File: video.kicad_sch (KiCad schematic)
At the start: 89 parts, among them Q10 2N3906, Q4 2N3906, Q5 2N3906, Q6 2N3906, Q7 2N3906, Q8 2N3906, Q9 2N3906

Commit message: prepare for fabrication
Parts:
- C41, C42, C51, C52, C53, C61: LCSC (none) -> C46653; LCSC Part (none) -> C46653
- C43, C44, C63, C72, C81: LCSC (none) -> C344201; LCSC Part (none) -> C344201
- C45, C54, C55, C56, C57, C58: LCSC (none) -> C113833; LCSC Part (none) -> C113833
- C46, C47, C48: LCSC (none) -> C107154; LCSC Part (none) -> C107154
- Q10, Q4, Q5, Q6, Q7, Q8, Q9: LCSC (none) -> C49023424; LCSC Part (none) -> C49023424
- R22, R24, R25, R26, R35, R36, R38, R39: LCSC (none) -> C2907326; LCSC Part (none) -> C2907326
- R23: LCSC (none) -> C2907216; LCSC Part (none) -> C2907216
- R27, R29, R31, R33, R37, R41, R53, R54: LCSC (none) -> C137498; LCSC Part (none) -> C137498
- R28, R40, R55: LCSC (none) -> C17540; LCSC Part (none) -> C17540
- R30, R32, R34: LCSC (none) -> C17634; LCSC Part (none) -> C17634
- R42, R43, R44, R45, R47: LCSC (none) -> C4368; LCSC Part (none) -> C4368
- R46: LCSC (none) -> C2907268; LCSC Part (none) -> C2907268
- R48: LCSC (none) -> C149504; LCSC Part (none) -> C149504
- R57, R58, R59: LCSC (none) -> C2483588; LCSC Part (none) -> C2483588
- R70: LCSC (none) -> C2907219; LCSC Part (none) -> C2907219
- TP16, TP17, TP18, TP19, TP20, TP21, TP22, TP23, TP24, TP25, TP26, TP28, TP29, TP41: now not fitted

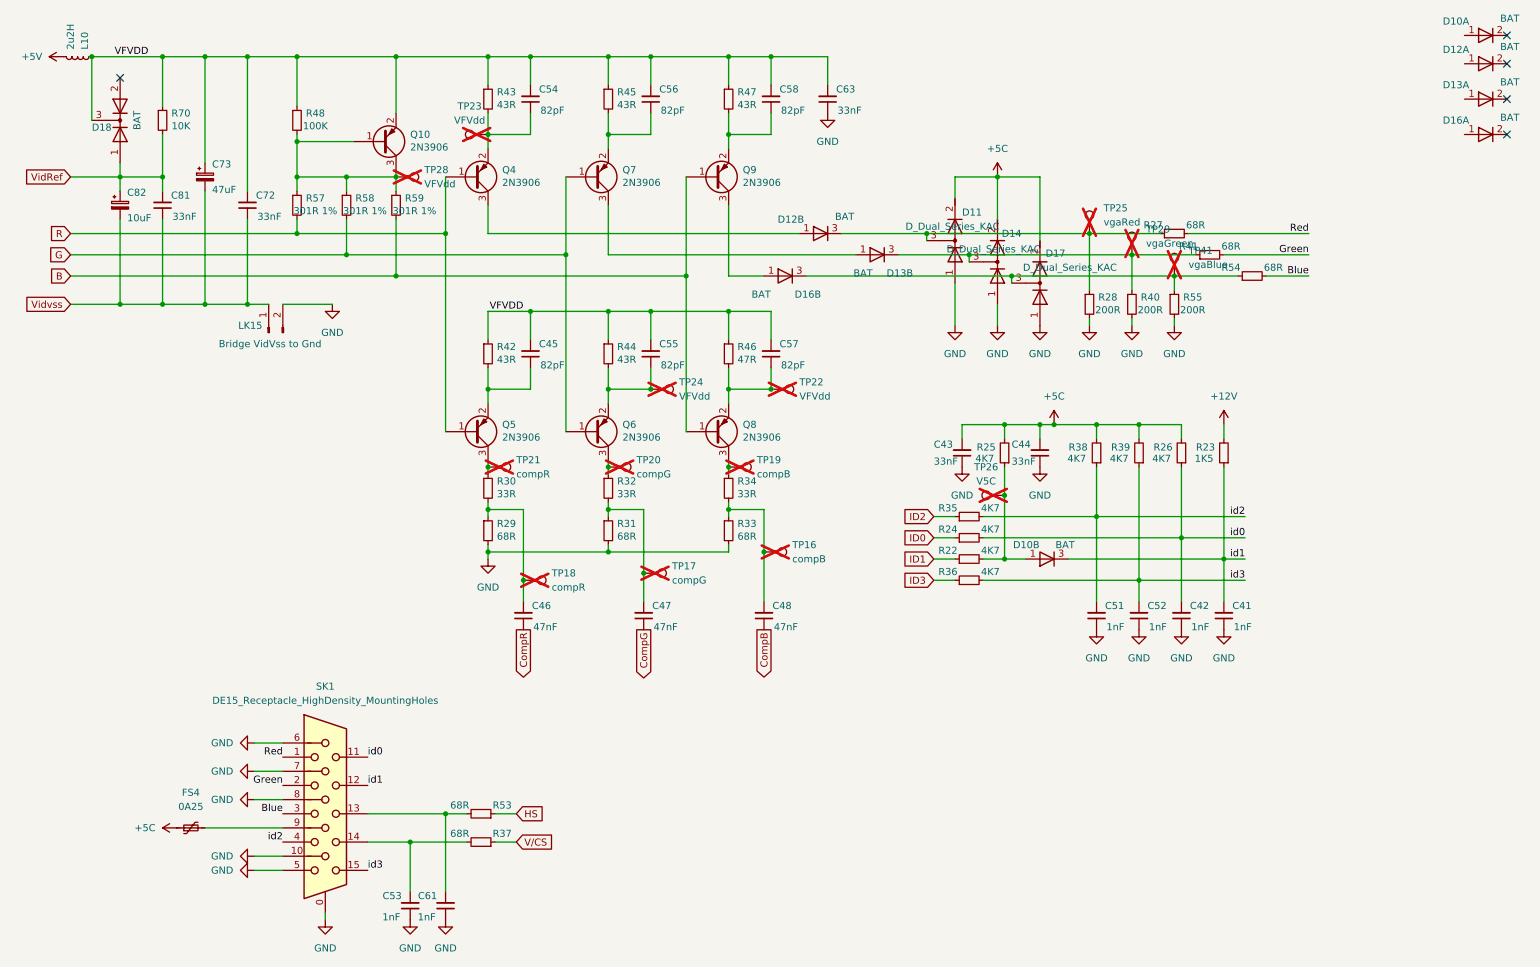
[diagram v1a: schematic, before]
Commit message: verify all component values vs TRM
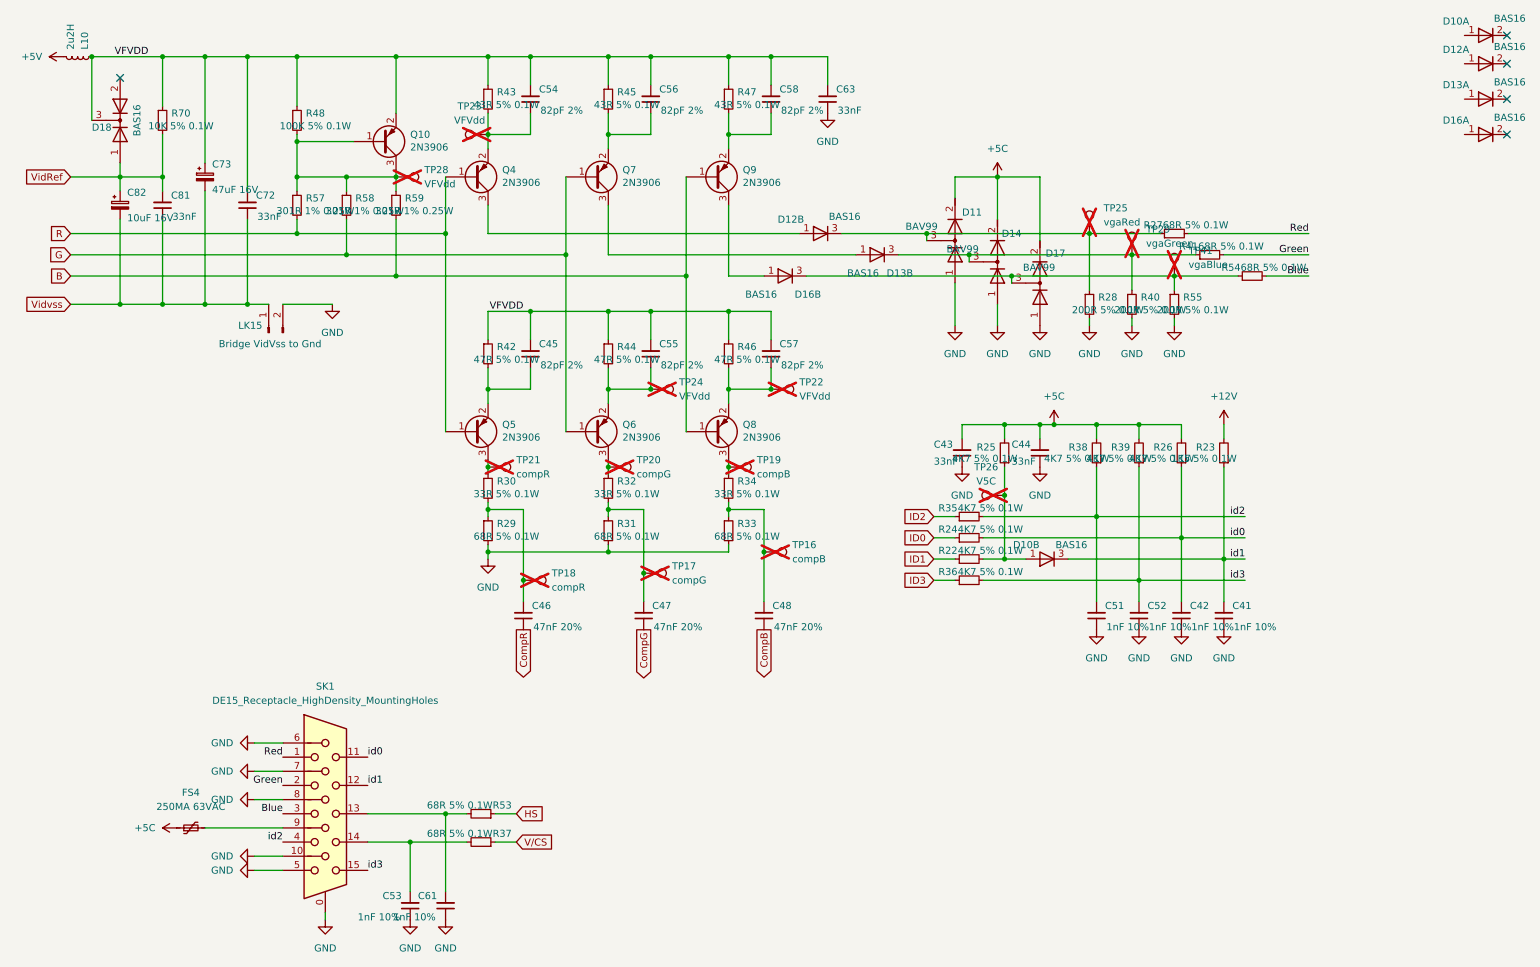
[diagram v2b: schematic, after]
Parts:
- C41, C42, C51, C52, C53, C61: value 1nF -> 1nF 10%
- C45, C54, C55, C56, C57, C58: value 82pF -> 82pF 2%
- C46, C47, C48: value 47nF -> 47nF 20%
- C73: value 47uF -> 47uF 16V
- C82: value 10uF -> 10uF 16V
- D10, D12, D13, D16, D18: value BAT -> BAS16
- D11, D14, D17: value D_Dual_Series_KAC -> BAV99
- FS4: value 0A25 -> 250MA 63VAC
- R22, R24, R25, R26, R35, R36, R38, R39: value 4K7 -> 4K7 5% 0.1W
- R23: value 1K5 -> 1K5 5% 0.1W
- R27, R29, R31, R33, R37, R41, R53, R54: value 68R -> 68R 5% 0.1W
- R28, R40, R55: value 200R -> 200R 5% 0.1W
- R30, R32, R34: value 33R -> 33R 5% 0.1W
- R42, R44: value 43R -> 47R 5% 0.1W
- R43, R45, R47: value 43R -> 43R 5% 0.1W
- R46: value 47R -> 47R 5% 0.1W
- R48: value 100K -> 100K 5% 0.1W
- R57, R58, R59: value 301R 1% -> 301R 1% 0.25W
- R70: value 10K -> 10K 5% 0.1W
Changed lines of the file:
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@@
 			)
 		)
-		(property "Value" "68R"
+		(property "Value" "68R 5% 0.1W"
 			(at 238.76 56.896 90)
 			(effects
@@
 			)
 		)
-		(property "Value" "BAT"
+		(property "Value" "BAS16"
 			(at 281.178 17.272 0)
 			(effects
@@
 			)
 		)
-		(property "Value" "1nF"
+		(property "Value" "1nF 10%"
 			(at 208.788 121.412 0)
 			(effects
@@
 			)
 		)
-		(property "Value" "1nF"
+		(property "Value" "1nF 10%"
 			(at 88.392 173.482 0)
 			(effects
@@
 			)
 		)
-		(property "Value" "D_Dual_Series_KAC"
+		(property "Value" "BAV99"
 			(at 193.802 56.896 90)
 			(effects
@@
 			)
 		)
-		(property "Value" "1nF"
+		(property "Value" "1nF 10%"
 			(at 216.408 121.412 0)
 			(effects
@@
 			)
 		)
-		(property "Value" "47nF"
+		(property "Value" "47nF 20%"
 			(at 127.508 121.412 0)
 			(effects
@@
 			)
 		)
-		(property "Value" "BAT"
+		(property "Value" "BAS16"
 			(at 199.644 106.68 0)
 			(effects
@@
 			)
 		)
-		(property "Value" "10uF"
+		(property "Value" "10uF 16V"
 			(at 33.02 48.006 0)
 			(effects
@@
 			)
 		)
-		(property "Value" "43R"
+		(property "Value" "47R 5% 0.1W"
 			(at 101.092 73.406 0)
 			(effects
@@
 			)
 		)
-		(property "Value" "BAT"
+		(property "Value" "BAS16"
 			(at 161.798 47.752 0)
 			(effects
@@
 			)
 		)
-		(property "Value" "BAT"
+		(property "Value" "BAS16"
 			(at 165.1 57.912 0)
 			(effects
@@
 			)
 		)
-		(property "Value" "200R"
+		(property "Value" "200R 5% 0.1W"
 			(at 209.042 64.516 0)
 			(effects
@@
 			)
 		)
-		(property "Value" "47nF"
+		(property "Value" "47nF 20%"
 			(at 149.098 121.412 0)
 			(effects
@@
 			)
 		)
-		(property "Value" "43R"
+		(property "Value" "43R 5% 0.1W"
 			(at 101.092 27.686 0)
 			(effects
@@
 			)
 		)
-		(property "Value" "D_Dual_Series_KAC"
+		(property "Value" "BAV99"
 			(at 172.72 49.53 90)
 			(effects
@@
 			)
 		)
-		(property "Value" "47nF"
+		(property "Value" "47nF 20%"
 			(at 105.918 121.412 0)
 			(effects
@@
 			)
 		)
-		(property "Value" "82pF"
+		(property "Value" "82pF 2%"
 			(at 107.188 74.422 0)
 			(effects
@@
 			)
 		)
-		(property "Value" "4K7"
+		(property "Value" "4K7 5% 0.1W"
 			(at 203.454 91.186 0)
 			(effects
@@
 			)
 		)
-		(property "Value" "D_Dual_Series_KAC"
+		(property "Value" "BAV99"
 			(at 180.086 53.594 90)
 			(effects
@@
 			)
 		)
-		(property "Value" "68R"
+		(property "Value" "68R 5% 0.1W"
 			(at 144.272 105.156 0)
 			(effects
@@
 			)
 		)
-		(property "Value" "43R"
+		(property "Value" "43R 5% 0.1W"
 			(at 144.272 27.686 0)
 			(effects
@@
 			)
 		)
-		(property "Value" "301R 1%"
+		(property "Value" "301R 1% 0.25W"
 			(at 75.692 46.736 0)
 			(effects
@@
 			)
 		)
-		(property "Value" "47R"
+		(property "Value" "47R 5% 0.1W"
 			(at 144.272 73.406 0)
 			(effects
@@
 			)
 		)
-		(property "Value" "82pF"
+		(property "Value" "82pF 2%"
 			(at 128.778 28.702 0)
 			(effects
@@
 			)
 		)
-		(property "Value" "82pF"
+		(property "Value" "82pF 2%"
 			(at 107.188 28.702 0)
 			(effects
@@
 			)
 		)
-		(property "Value" "BAT"
+		(property "Value" "BAS16"
 			(at 281.178 29.972 0)
 			(effects
@@
 			)
 		)
-		(property "Value" "68R"
+		(property "Value" "68R 5% 0.1W"
 			(at 224.79 49.276 90)
 			(effects
@@
 			)
 		)
-		(property "Value" "301R 1%"
+		(property "Value" "301R 1% 0.25W"
 			(at 66.802 46.736 0)
 			(effects
@@
 			)
 		)
-		(property "Value" "68R"
+		(property "Value" "68R 5% 0.1W"
 			(at 92.71 153.416 90)
 			(effects
@@
 			)
 		)
-		(property "Value" "68R"
+		(property "Value" "68R 5% 0.1W"
 			(at 122.682 105.156 0)
 			(effects
@@
 			)
 		)
-		(property "Value" "4K7"
+		(property "Value" "4K7 5% 0.1W"
 			(at 187.96 107.696 90)
 			(effects
@@
 			)
 		)
-		(property "Value" "200R"
+		(property "Value" "200R 5% 0.1W"
 			(at 224.282 64.516 0)
 			(effects
@@
 			)
 		)
-		(property "Value" "BAT"
+		(property "Value" "BAS16"
 			(at 281.178 23.622 0)
 			(effects
@@
 			)
 		)
-		(property "Value" "4K7"
+		(property "Value" "4K7 5% 0.1W"
 			(at 218.694 91.186 0)
 			(effects
@@
 			)
 		)
-		(property "Value" "82pF"
+		(property "Value" "82pF 2%"
 			(at 128.778 74.422 0)
 			(effects
@@
 			)
 		)
-		(property "Value" "301R 1%"
+		(property "Value" "301R 1% 0.25W"
 			(at 84.582 46.736 0)
 			(effects
@@
 			)
 		)
-		(property "Value" "BAT"
+		(property "Value" "BAS16"
 			(at 34.798 30.48 0)
 			(effects
@@
 			)
 		)
-		(property "Value" "1nF"
+		(property "Value" "1nF 10%"
 			(at 231.648 121.412 0)
 			(effects
@@
 			)
 		)
-		(property "Value" "4K7"
+		(property "Value" "4K7 5% 0.1W"
 			(at 187.96 103.886 90)
 			(effects
@@
 			)
 		)
-		(property "Value" "33R"
+		(property "Value" "33R 5% 0.1W"
 			(at 122.682 97.536 0)
 			(effects
@@
 			)
 		)
-		(property "Value" "4K7"
+		(property "Value" "4K7 5% 0.1W"
 			(at 186.944 91.186 0)
 			(effects
@@
 			)
 		)
-		(property "Value" "0A25"
+		(property "Value" "250MA 63VAC"
 			(at 44.45 153.67 90)
 			(effects
@@
 			)
 		)
-		(property "Value" "47uF"
+		(property "Value" "47uF 16V"
 			(at 48.26 42.926 0)
 			(effects
@@
 			)
 		)
-		(property "Value" "43R"
+		(property "Value" "47R 5% 0.1W"
 			(at 122.682 73.406 0)
 			(effects
@@
 			)
 		)
-		(property "Value" "10K"
+		(property "Value" "10K 5% 0.1W"
 			(at 42.672 31.496 0)
 			(effects
@@
 			)
 		)
-		(property "Value" "82pF"
+		(property "Value" "82pF 2%"
 			(at 150.368 74.422 0)
 			(effects
@@
 			)
 		)
-		(property "Value" "1K5"
+		(property "Value" "1K5 5% 0.1W"
 			(at 226.314 91.186 0)
 			(effects
@@
 			)
 		)
-		(property "Value" "33R"
+		(property "Value" "33R 5% 0.1W"
 			(at 144.272 97.536 0)
 			(effects
@@
 			)
 		)
-		(property "Value" "100K"
+		(property "Value" "100K 5% 0.1W"
 			(at 66.802 31.496 0)
 			(effects
@@
 			)
 		)
-		(property "Value" "1nF"
+		(property "Value" "1nF 10%"
 			(at 82.042 173.482 0)
 			(effects
@@
 			)
 		)
-		(property "Value" "4K7"
+		(property "Value" "4K7 5% 0.1W"
 			(at 187.96 100.076 90)
 			(effects
@@
 			)
 		)
-		(property "Value" "BAT"
+		(property "Value" "BAS16"
 			(at 146.812 61.722 0)
 			(effects
@@
 			)
 		)
-		(property "Value" "1nF"
+		(property "Value" "1nF 10%"
 			(at 224.028 121.412 0)
 			(effects
@@
 			)
 		)
-		(property "Value" "82pF"
+		(property "Value" "82pF 2%"
 			(at 150.368 28.702 0)
 			(effects
@@
 			)
 		)
-		(property "Value" "33R"
+		(property "Value" "33R 5% 0.1W"
 			(at 101.092 97.536 0)
 			(effects
@@
 			)
 		)
-		(property "Value" "68R"
+		(property "Value" "68R 5% 0.1W"
 			(at 231.14 53.086 90)
 			(effects
@@
 			)
 		)
-		(property "Value" "4K7"
+		(property "Value" "4K7 5% 0.1W"
 			(at 211.074 91.186 0)
 			(effects
@@
 			)
 		)
-		(property "Value" "68R"
+		(property "Value" "68R 5% 0.1W"
 			(at 92.71 158.496 90)
 			(effects
@@
 			)
 		)
-		(property "Value" "68R"
+		(property "Value" "68R 5% 0.1W"
 			(at 101.092 105.156 0)
 			(effects
@@
 			)
 		)
-		(property "Value" "4K7"
+		(property "Value" "4K7 5% 0.1W"
 			(at 187.96 111.506 90)
 			(effects
@@
 			)
 		)
-		(property "Value" "200R"
+		(property "Value" "200R 5% 0.1W"
 			(at 216.662 64.516 0)
 			(effects
@@
 			)
 		)
-		(property "Value" "43R"
+		(property "Value" "43R 5% 0.1W"
 			(at 122.682 27.686 0)
 			(effects
@@
 			)
 		)
-		(property "Value" "BAT"
+		(property "Value" "BAS16"
 			(at 281.178 12.192 0)
 			(effects

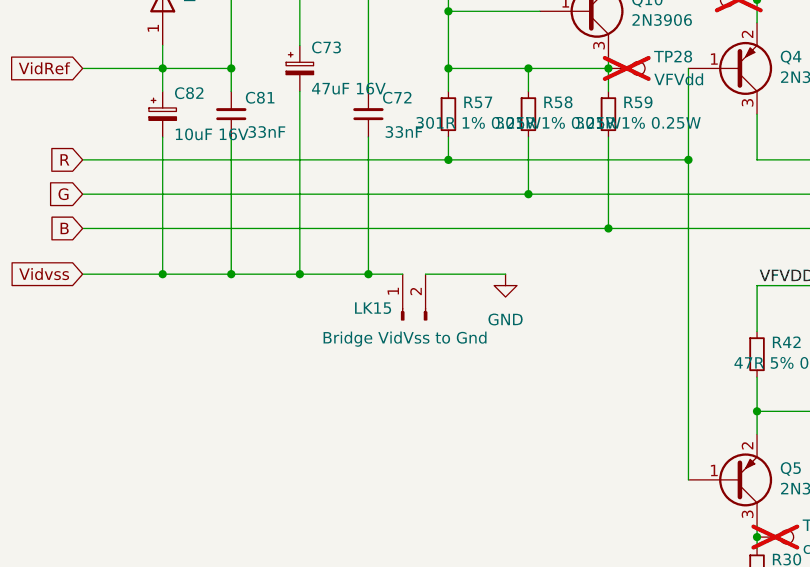
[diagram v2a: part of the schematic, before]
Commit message: switch links to net ties
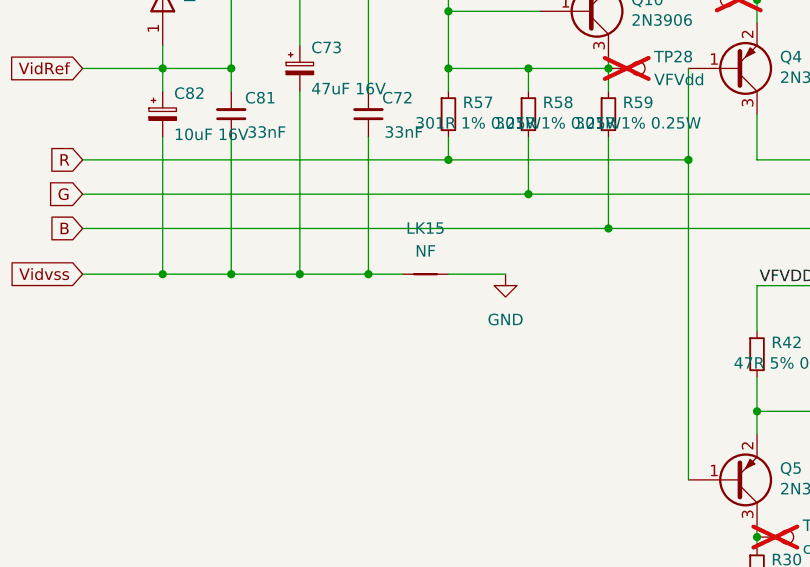
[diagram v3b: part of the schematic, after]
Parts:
- removed LK15: Bridge VidVss to Gnd, Connector_PinHeader_2.54mm:PinHeader_1x02_P2.54mm_Vertical, symbol Connector:Conn_01x02_Pin
- added LK15: NF, Acorn:Link_Connected, symbol Device:NetTie_2
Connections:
- net GND: now also LK15.2
- net Vidvss: now also LK15.1
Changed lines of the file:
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@@
 	(wire
 		(pts
+			(xy 63.5 63.5) (xy 69.85 63.5)
+		)
+		(stroke
+			(width 0)
+			(type default)
+		)
+	)
+	(wire
+		(pts
 			(xy 54.61 48.26) (xy 54.61 63.5)
 		)
@@
 	(wire
 		(pts
-			(xy 60.96 63.5) (xy 69.85 63.5)
-		)
-		(stroke
-			(width 0)
-			(type default)
-		)
-	)
-	(wire
-		(pts
 			(xy 90.17 168.91) (xy 90.17 154.94)
 		)
@@
 	)
 	(symbol
-		(lib_id "Connector:Conn_01x02_Pin")
-		(at 58.42 68.58 90)
-		(unit 1)
-		(exclude_from_sim no)
-		(in_bom yes)
-		(on_board yes)
-		(dnp no)
-		(property "Reference" "LK15"
-			(at 55.118 67.31 90)
-			(effects
-				(font
-					(size 1.27 1.27)
-				)
-			)
-		)
-		(property "Value" "Bridge VidVss to Gnd"
-			(at 58.674 70.612 90)
-			(effects
-				(font
-					(size 1.27 1.27)
-				)
-			)
-		)
-		(property "Footprint" "Connector_PinHeader_2.54mm:PinHeader_1x02_P2.54mm_Vertical"
-			(at 58.42 68.58 0)
-			(effects
-				(font
-					(size 1.27 1.27)
-				)
-				(hide yes)
-			)
-		)
-		(property "Datasheet" "~"
-			(at 58.42 68.58 0)
-			(effects
-				(font
-					(size 1.27 1.27)
-				)
-				(hide yes)
-			)
-		)
-		(property "Description" "Generic connector, single row, 01x02, script generated"
-			(at 58.42 68.58 0)
-			(effects
-				(font
-					(size 1.27 1.27)
-				)
-				(hide yes)
-			)
-		)
-		(pin "2"
-		)
-		(pin "1"
-		)
-		(instances
-			(project "Acorn-A3010"
-				(path "/999882f3-94f8-4a89-9093-27a47d0cb289/21031065-42cd-49d4-b299-d2e76b62bbd8"
-					(reference "LK15")
-					(unit 1)
-				)
-			)
-		)
-	)
-	(symbol
 		(lib_id "Device:C_Small")
 		(at 105.41 26.67 180)
@@
 					(unit 1)
 				)
+			)
+		)
+	)
+	(symbol
+		(lib_id "Device:NetTie_2")
+		(at 60.96 63.5 0)
+		(unit 1)
+		(exclude_from_sim no)
+		(in_bom no)
+		(on_board yes)
+		(dnp no)
+		(fields_autoplaced yes)
+		(property "Reference" "LK15"
+			(at 60.96 58.42 0)
+			(effects
+				(font
+					(size 1.27 1.27)
+				)
+			)
+		)
+		(property "Value" "NF"
+			(at 60.96 60.96 0)
+			(effects
+				(font
+					(size 1.27 1.27)
+				)
+			)
+		)
+		(property "Footprint" "Acorn:Link_Connected"
+			(at 60.96 63.5 0)
+			(effects
+				(font
+					(size 1.27 1.27)
+				)
+				(hide yes)
+			)
+		)
+		(property "Datasheet" "~"
+			(at 60.96 63.5 0)
+			(effects
+				(font
+					(size 1.27 1.27)
+				)
+				(hide yes)
+			)
+		)
+		(property "Description" "Bridge VidVss to Gnd"
+			(at 60.96 63.5 0)
+			(effects
+				(font
+					(size 1.27 1.27)
+				)
+				(hide yes)
+			)
+		)
+		(pin "2"
+		)
+		(pin "1"
+		)
+		(instances
+			(project "Acorn-A3010"
+				(path "/999882f3-94f8-4a89-9093-27a47d0cb289/21031065-42cd-49d4-b299-d2e76b62bbd8"
+					(reference "LK15")
+					(unit 1)
+				)

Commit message: use handsolder footprints for fuses
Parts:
- FS4: footprint Fuse:Fuse_2512_6332Metric -> Fuse:Fuse_2512_6332Metric_Pad1.52x3.35mm_HandSolder
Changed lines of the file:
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@@
 			)
 		)
-		(property "Footprint" "Fuse:Fuse_2512_6332Metric"
+		(property "Footprint" "Fuse:Fuse_2512_6332Metric_Pad1.52x3.35mm_HandSolder"
 			(at 49.53 156.21 0)
 			(effects

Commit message: revise cap footprint selection
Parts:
- C73: footprint Capacitor_THT:CP_Radial_Tantal_D9.0mm_P5.00mm -> Capacitor_THT:CP_Radial_D8.0mm_P5.00mm
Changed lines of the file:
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@@
 			)
 		)
-		(property "Footprint" "Capacitor_THT:CP_Radial_Tantal_D9.0mm_P5.00mm"
+		(property "Footprint" "Capacitor_THT:CP_Radial_D8.0mm_P5.00mm"
 			(at 46.99 40.64 0)
 			(effects

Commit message: fix VGA port footprint
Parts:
- SK1: footprint Connector_Dsub:DSUB-15-HD_Female_Horizontal_P2.29x1.98mm_EdgePinOffset8.35mm_Housed_MountingHolesOffset10.89mm -> Connector_Dsub:DSUB-15-HD_Socket_Horizontal_P2.29x2.54mm_EdgePinOffset8.35mm_Housed_MountingHolesOffset10.89mm
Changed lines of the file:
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@@
 			)
 		)
-		(property "Footprint" "Connector_Dsub:DSUB-15-HD_Female_Horizontal_P2.29x1.98mm_EdgePinOffset8.35mm_Housed_MountingHolesOffset10.89mm"
+		(property "Footprint" "Connector_Dsub:DSUB-15-HD_Socket_Horizontal_P2.29x2.54mm_EdgePinOffset8.35mm_Housed_MountingHolesOffset10.89mm"
 			(at 44.45 144.78 0)
 			(effects
